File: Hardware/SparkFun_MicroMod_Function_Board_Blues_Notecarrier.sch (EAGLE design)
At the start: 68 parts, among them J2 MICROMOD_FUNCTION_STANDARD, J6 NOTECARD, Q1 220mA/50V/3.5Ω, Q2 20V/4.2A/52mΩ/1.4W, Q3 220mA/50V/3.5Ω, Q4 20V/4.2A/52mΩ/1.4W, Q5 220mA/50V/3.5Ω, Q6 20V/4.2A/52mΩ/1.4W, U1 EEPROM, U2 TCR2EF33

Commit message: Swap Notecard RX/TX, add missing silk, add diode PROD-ID.
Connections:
- net NOTECARD_RX: now also J2.RX; no longer J2.TX
- net NOTECARD_TX: now also J2.TX; no longer J2.RX
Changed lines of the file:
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@@
 <setting verticaltext="up"/>
 </settings>
-<grid distance="0.1" unitdist="inch" unit="inch" style="lines" multiple="1" display="yes" altdistance="0.01" altunitdist="inch" altunit="inch"/>
+<grid distance="0.1" unitdist="inch" unit="inch" style="lines" multiple="1" display="no" altdistance="0.01" altunitdist="inch" altunit="inch"/>
 <layers>
 <layer number="1" name="Top" color="4" fill="1" visible="no" active="no"/>
@@
 </segment>
 <segment>
+<wire x1="127" y1="137.16" x2="124.46" y2="137.16" width="0.1524" layer="91"/>
+<label x="127" y="137.16" size="1.27" layer="95" font="vector" xref="yes"/>
+<pinref part="J2" gate="J1" pin="RX"/>
+</segment>
+</net>
+<net name="NOTECARD_TX" class="0">
+<segment>
+<wire x1="335.28" y1="129.54" x2="332.74" y2="129.54" width="0.1524" layer="91"/>
+<label x="335.28" y="129.54" size="1.27" layer="95" font="vector" xref="yes"/>
+<pinref part="J6" gate="G$1" pin="TX"/>
+</segment>
+<segment>
 <wire x1="127" y1="134.62" x2="124.46" y2="134.62" width="0.1524" layer="91"/>
 <label x="127" y="134.62" size="1.27" layer="95" font="vector" xref="yes"/>
@@
 </segment>
 </net>
-<net name="NOTECARD_TX" class="0">
-<segment>
-<wire x1="335.28" y1="129.54" x2="332.74" y2="129.54" width="0.1524" layer="91"/>
-<label x="335.28" y="129.54" size="1.27" layer="95" font="vector" xref="yes"/>
-<pinref part="J6" gate="G$1" pin="TX"/>
-</segment>
-<segment>
-<wire x1="127" y1="137.16" x2="124.46" y2="137.16" width="0.1524" layer="91"/>
-<label x="127" y="137.16" size="1.27" layer="95" font="vector" xref="yes"/>
-<pinref part="J2" gate="J1" pin="RX"/>
-</segment>
-</net>

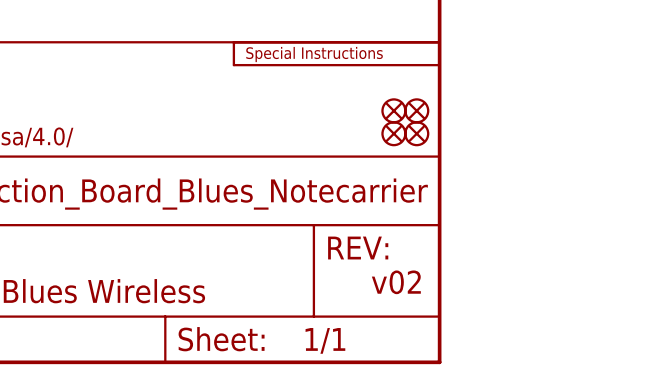
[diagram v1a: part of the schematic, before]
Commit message: Rev to v10. Update RGB Silk. Repanelize for changes.
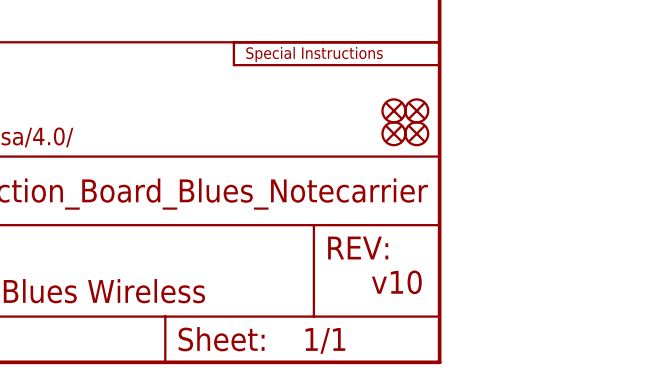
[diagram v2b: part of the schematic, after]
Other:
- note added: "v10"
- note removed: "v02"
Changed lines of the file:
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@@
 <text x="350.52" y="11.43" size="2.54" layer="94" font="vector">Alex Brudner</text>
 <text x="331.724" y="6.604" size="2.54" layer="94" font="vector">Based on a design by: E. Pierce, Blues Wireless</text>
-<text x="424.18" y="7.62" size="2.54" layer="94" font="vector">v02</text>
+<text x="424.18" y="7.62" size="2.54" layer="94" font="vector">v10</text>
 <text x="106.934" y="180.086" size="2.54" layer="94" font="vector" align="center">MicroMod Function Connector</text>
 <text x="178.054" y="263.906" size="2.54" layer="94" font="vector" align="center">Power Control</text>

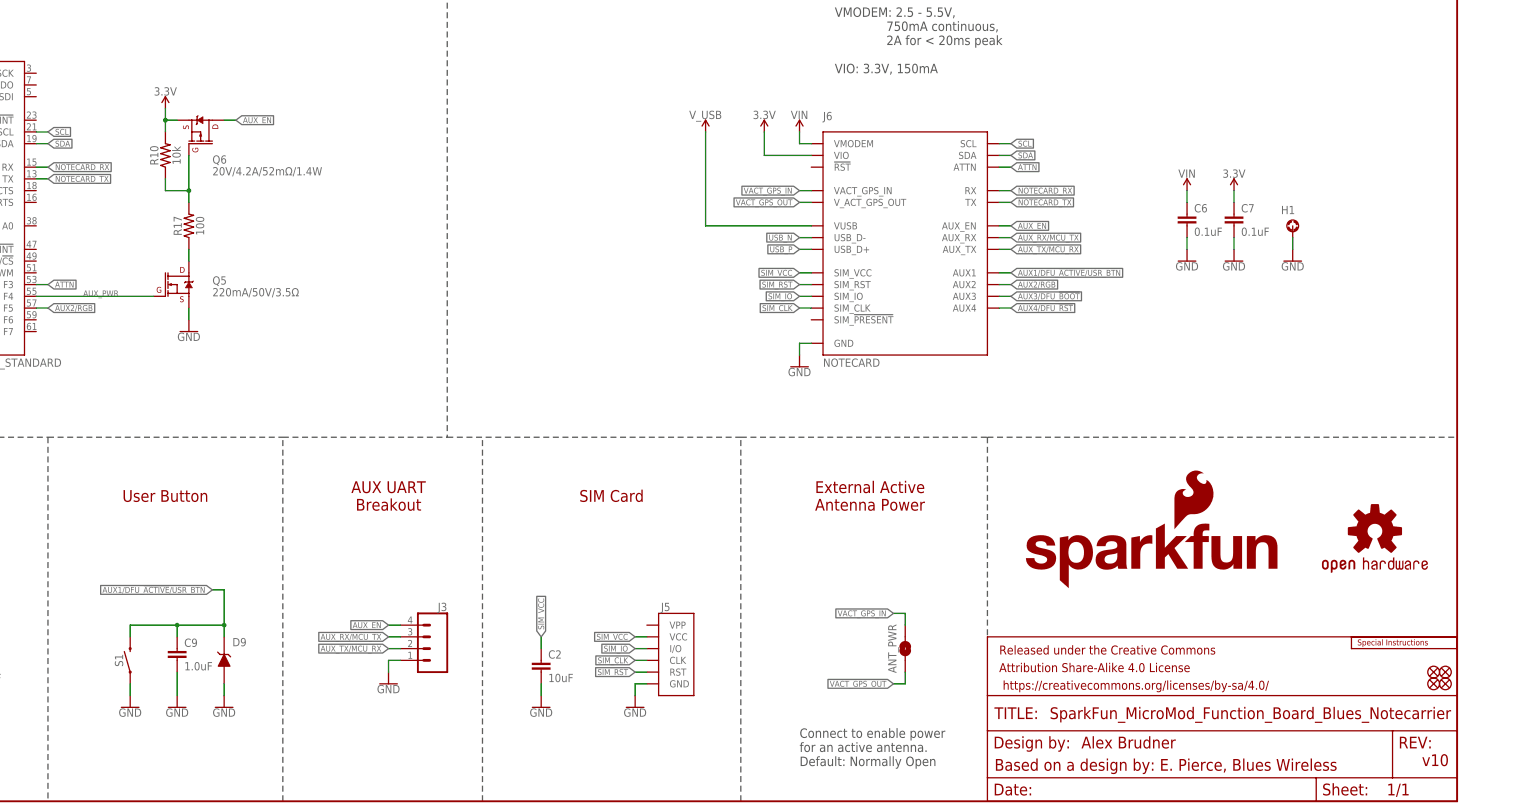
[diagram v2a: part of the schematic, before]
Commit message: Rev v11
AEN wasn't enabled by default because it was missing a passive. Added passive and rerouted.
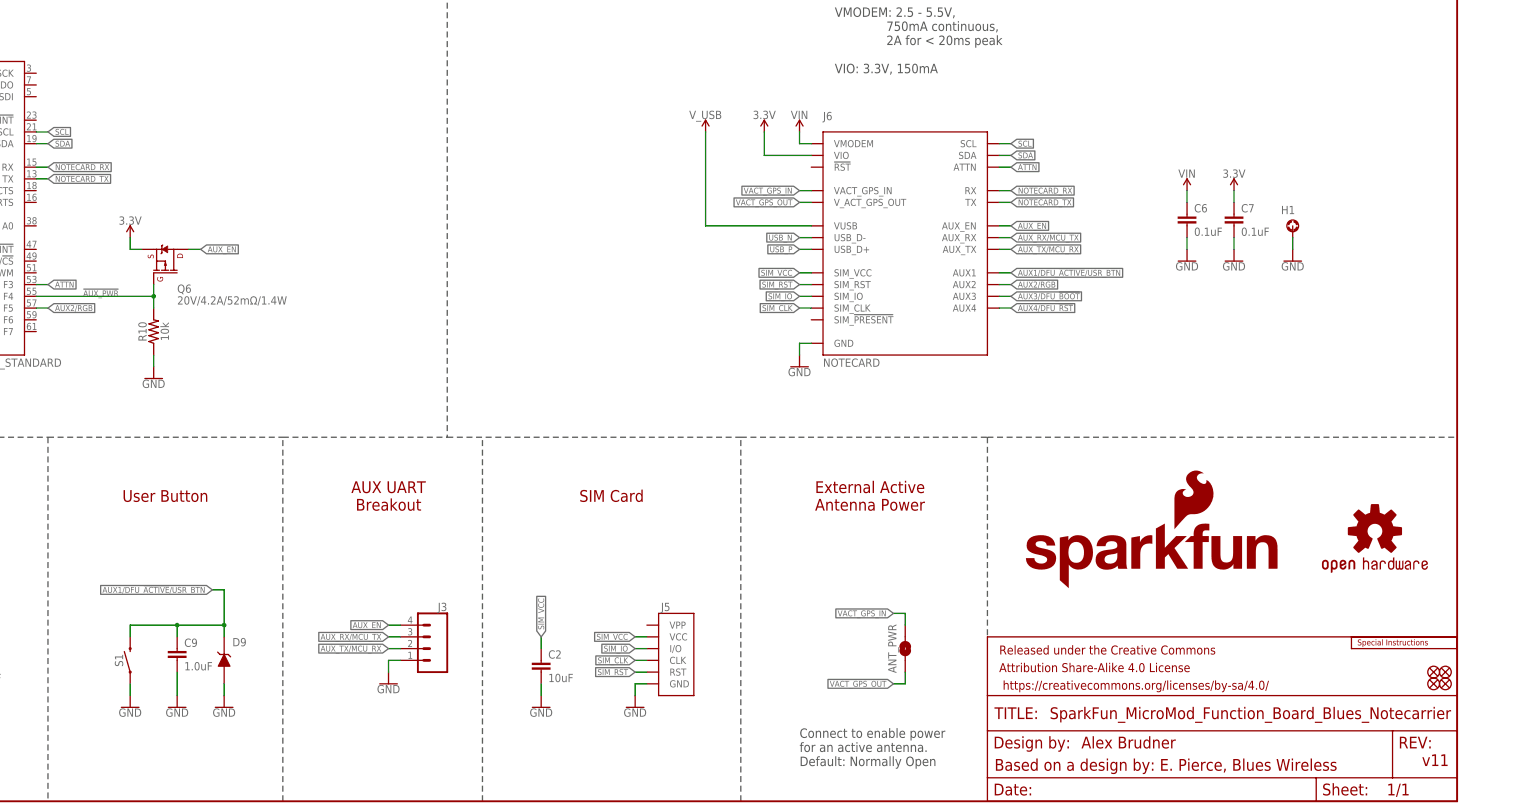
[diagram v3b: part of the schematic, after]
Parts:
- removed Q5: 220mA/50V/3.5Ω, SparkFun-DiscreteSemi:MOSFET-NCH-BSS138
- removed R17: 100, SparkFun-Resistors:100OHM-0402-TIGHT-1/16W-1%
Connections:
- removed net AUX_PWR: J2.F4, Q5.G
- removed net N$19: Q6.G, R10.1, R17.2
- removed net N$20: Q5.D, R17.1
- new net !AUX_PWR!: J2.F4, Q6.G, R10.2
- net 3.3V: no longer R10.2
- net GND: now also R10.1; no longer Q5.S
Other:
- note added: "v11"
- note removed: "v10"
- moved on the sheet: Q6, R10
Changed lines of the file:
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@@
 <part name="SUPPLY21" library="SparkFun-PowerSymbols" deviceset="3.3V" device=""/>
 <part name="RGB" library="SparkFun-Jumpers" deviceset="JUMPER-SMT_2_NC_TRACE" device="_SILK" package3d_urn="urn:adsk.eagle:package:39281/1"/>
-<part name="Q5" library="SparkFun-DiscreteSemi" deviceset="MOSFET-NCH" device="-BSS138" value="220mA/50V/3.5Ω"/>
 <part name="Q6" library="SparkFun-DiscreteSemi" deviceset="MOSFET_PCH" device="-DMG2305UX-7" value="20V/4.2A/52mΩ/1.4W"/>
+<part name="GND33" library="SparkFun-PowerSymbols" deviceset="GND" device=""/>
+<part name="SUPPLY17" library="SparkFun-PowerSymbols" deviceset="3.3V" device=""/>
 <part name="R10" library="SparkFun-Resistors" deviceset="10KOHM" device="-0402T-1/16W-1%" value="10k"/>
-<part name="GND33" library="SparkFun-PowerSymbols" deviceset="GND" device=""/>
-<part name="R17" library="SparkFun-Resistors" deviceset="100OHM" device="-0402-TIGHT-1/16W-1%" value="100"/>
-<part name="SUPPLY17" library="SparkFun-PowerSymbols" deviceset="3.3V" device=""/>
 </parts>
 <sheets>
@@
 <text x="350.52" y="11.43" size="2.54" layer="94" font="vector">Alex Brudner</text>
 <text x="331.724" y="6.604" size="2.54" layer="94" font="vector">Based on a design by: E. Pierce, Blues Wireless</text>
-<text x="424.18" y="7.62" size="2.54" layer="94" font="vector">v10</text>
+<text x="424.18" y="7.62" size="2.54" layer="94" font="vector">v11</text>
 <text x="106.934" y="180.086" size="2.54" layer="94" font="vector" align="center">MicroMod Function Connector</text>
 <text x="178.054" y="263.906" size="2.54" layer="94" font="vector" align="center">Power Control</text>
@@
 <attribute name="VALUE" x="94.488" y="45.72" size="1.778" layer="96" font="vector" rot="R90" align="center" display="off"/>
 </instance>
-<instance part="Q5" gate="NMOS" x="154.94" y="111.76" smashed="yes">
-<attribute name="NAME" x="162.56" y="111.76" size="1.778" layer="95" font="vector"/>
-<attribute name="VALUE" x="162.56" y="109.22" size="1.778" layer="96" font="vector"/>
-</instance>
-<instance part="Q6" gate="G$1" x="160.02" y="144.78" smashed="yes" rot="MR90">
-<attribute name="NAME" x="162.56" y="139.7" size="1.778" layer="95" font="vector" rot="MR180"/>
-<attribute name="VALUE" x="162.56" y="137.16" size="1.778" layer="96" font="vector" rot="MR180"/>
-</instance>
-<instance part="R10" gate="G$1" x="152.4" y="139.7" smashed="yes" rot="R90">
-<attribute name="NAME" x="150.876" y="139.7" size="1.778" layer="95" font="vector" rot="R90" align="bottom-center"/>
-<attribute name="VALUE" x="153.924" y="139.7" size="1.778" layer="96" font="vector" rot="R90" align="top-center"/>
-</instance>
-<instance part="GND33" gate="1" x="157.48" y="101.6" smashed="yes">
-<attribute name="VALUE" x="157.48" y="101.346" size="1.778" layer="96" font="vector" align="top-center"/>
-</instance>
-<instance part="R17" gate="G$1" x="157.48" y="124.46" smashed="yes" rot="R90">
-<attribute name="NAME" x="155.956" y="124.46" size="1.778" layer="95" font="vector" rot="R90" align="bottom-center"/>
-<attribute name="VALUE" x="159.004" y="124.46" size="1.778" layer="96" font="vector" rot="R90" align="top-center"/>
-</instance>
-<instance part="SUPPLY17" gate="G$1" x="152.4" y="149.86" smashed="yes">
-<attribute name="VALUE" x="152.4" y="152.654" size="1.778" layer="96" font="vector" align="bottom-center"/>
+<instance part="Q6" gate="G$1" x="152.4" y="116.84" smashed="yes" rot="MR90">
+<attribute name="NAME" x="154.94" y="111.76" size="1.778" layer="95" font="vector" rot="MR180"/>
+<attribute name="VALUE" x="154.94" y="109.22" size="1.778" layer="96" font="vector" rot="MR180"/>
+</instance>
+<instance part="GND33" gate="1" x="149.86" y="91.44" smashed="yes">
+<attribute name="VALUE" x="149.86" y="91.186" size="1.778" layer="96" font="vector" align="top-center"/>
+</instance>
+<instance part="SUPPLY17" gate="G$1" x="144.78" y="121.92" smashed="yes">
+<attribute name="VALUE" x="144.78" y="124.714" size="1.778" layer="96" font="vector" align="bottom-center"/>
+</instance>
+<instance part="R10" gate="G$1" x="149.86" y="101.6" smashed="yes" rot="R90">
+<attribute name="NAME" x="148.336" y="101.6" size="1.778" layer="95" font="vector" rot="R90" align="bottom-center"/>
+<attribute name="VALUE" x="151.384" y="101.6" size="1.778" layer="96" font="vector" rot="R90" align="top-center"/>
 </instance>
 </instances>
@@
 </segment>
 <segment>
-<pinref part="Q5" gate="NMOS" pin="S"/>
-<wire x1="157.48" y1="106.68" x2="157.48" y2="104.14" width="0.1524" layer="91"/>
+<pinref part="R10" gate="G$1" pin="1"/>
 <pinref part="GND33" gate="1" pin="GND"/>
+<wire x1="149.86" y1="96.52" x2="149.86" y2="93.98" width="0.1524" layer="91"/>
 </segment>
 </net>
@@
 <segment>
 <pinref part="SUPPLY17" gate="G$1" pin="3.3V"/>
-<wire x1="152.4" y1="149.86" x2="152.4" y2="147.32" width="0.1524" layer="91"/>
-<pinref part="R10" gate="G$1" pin="2"/>
+<wire x1="144.78" y1="121.92" x2="144.78" y2="119.38" width="0.1524" layer="91"/>
 <pinref part="Q6" gate="G$1" pin="S"/>
-<wire x1="152.4" y1="147.32" x2="152.4" y2="144.78" width="0.1524" layer="91"/>
-<wire x1="154.94" y1="147.32" x2="152.4" y2="147.32" width="0.1524" layer="91"/>
-<junction x="152.4" y="147.32"/>
+<wire x1="147.32" y1="119.38" x2="144.78" y2="119.38" width="0.1524" layer="91"/>
 </segment>
 </net>
@@
 <segment>
 <pinref part="Q6" gate="G$1" pin="D"/>
-<wire x1="165.1" y1="147.32" x2="167.64" y2="147.32" width="0.1524" layer="91"/>
-<label x="167.64" y="147.32" size="1.27" layer="95" xref="yes"/>
+<wire x1="157.48" y1="119.38" x2="160.02" y2="119.38" width="0.1524" layer="91"/>
+<label x="160.02" y="119.38" size="1.27" layer="95" xref="yes"/>
 </segment>
 </net>
@@
 </segment>
 </net>
-<net name="AUX_PWR" class="0">
-<segment>
-<pinref part="Q5" gate="NMOS" pin="G"/>
+<net name="!AUX_PWR!" class="0">
+<segment>
 <pinref part="J2" gate="J1" pin="F4"/>
 <wire x1="149.86" y1="109.22" x2="124.46" y2="109.22" width="0.1524" layer="91"/>
 <label x="134.62" y="109.22" size="1.27" layer="95"/>
-</segment>
-</net>
-<net name="N$19" class="0">
-<segment>
 <pinref part="Q6" gate="G$1" pin="G"/>
-<wire x1="157.48" y1="139.7" x2="157.48" y2="132.08" width="0.1524" layer="91"/>
-<wire x1="157.48" y1="132.08" x2="152.4" y2="132.08" width="0.1524" layer="91"/>
-<wire x1="152.4" y1="132.08" x2="152.4" y2="134.62" width="0.1524" layer="91"/>
-<pinref part="R10" gate="G$1" pin="1"/>
-<pinref part="R17" gate="G$1" pin="2"/>
-<wire x1="157.48" y1="129.54" x2="157.48" y2="132.08" width="0.1524" layer="91"/>
-<junction x="157.48" y="132.08"/>
-</segment>
-</net>
-<net name="N$20" class="0">
-<segment>
-<pinref part="R17" gate="G$1" pin="1"/>
-<pinref part="Q5" gate="NMOS" pin="D"/>
-<wire x1="157.48" y1="119.38" x2="157.48" y2="116.84" width="0.1524" layer="91"/>
-</segment>
-</net>
+<wire x1="149.86" y1="111.76" x2="149.86" y2="109.22" width="0.1524" layer="91"/>
+<pinref part="R10" gate="G$1" pin="2"/>
+<wire x1="149.86" y1="109.22" x2="149.86" y2="106.68" width="0.1524" layer="91"/>
+<junction x="149.86" y="109.22"/>
+</segment>
+</net>

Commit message: Updated to replace EOL caps.
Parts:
- C3, C4: device SparkFun-Capacitors:100UF-POLAR-25V-20%(ELEC) -> SparkFun-Capacitors:100UF-POLAR-25V-20%-SMD(ELEC)
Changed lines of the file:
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@@
 <part name="D6" library="SparkFun-DiscreteSemi" deviceset="DIODE-SCHOTTKY" device="-BAT60A" value="3A/10V/280mV"/>
 <part name="MEAS" library="SparkFun-Jumpers" deviceset="JUMPER-COMBO_2_NC_TRACE" device=""/>
-<part name="C3" library="SparkFun-Capacitors" deviceset="100UF-POLAR" device="-25V-20%(ELEC)" value="100uF"/>
-<part name="C4" library="SparkFun-Capacitors" deviceset="100UF-POLAR" device="-25V-20%(ELEC)" value="100uF"/>
+<part name="C3" library="SparkFun-Capacitors" deviceset="100UF-POLAR" device="-25V-20%-SMD(ELEC)" value="100uF"/>
+<part name="C4" library="SparkFun-Capacitors" deviceset="100UF-POLAR" device="-25V-20%-SMD(ELEC)" value="100uF"/>
 <part name="GND15" library="SparkFun-PowerSymbols" deviceset="GND" device=""/>
 <part name="GND16" library="SparkFun-PowerSymbols" deviceset="GND" device=""/>

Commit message: DNP unused diode.
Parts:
- D9: value SMBJP6KE6.8A-TP -> SMBJP6KE-DNP; device SparkFun_MicroMod_Function_Board_Blues_Notecarrier:SMBJP6KE6.8A-TP -> SparkFun_MicroMod_Function_Board_Blues_Notecarrier:SMBJP6KE-DNP
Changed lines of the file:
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@@
 <part name="J3" library="SparkFun-Connectors" deviceset="CONN_04" device="1X04_NO_SILK_NO_POP"/>
 <part name="C9" library="SparkFun-Capacitors" deviceset="1.0UF" device="-0402T-16V-10%" value="1.0uF"/>
-<part name="D9" library="SparkFun_MicroMod_Function_Board_Blues_Notecarrier" deviceset="SMBJP6KE" device="6.8A-TP"/>
+<part name="D9" library="SparkFun_MicroMod_Function_Board_Blues_Notecarrier" deviceset="SMBJP6KE" device="-DNP" value="SMBJP6KE-DNP"/>
 <part name="GND29" library="SparkFun-PowerSymbols" deviceset="GND" device=""/>
 <part name="GND30" library="SparkFun-PowerSymbols" deviceset="GND" device=""/>
